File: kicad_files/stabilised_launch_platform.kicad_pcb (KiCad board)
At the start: 2 copper layers, 23 parts, among them J1 Conn_01x03_Male, J2 Conn_01x03_Male, J3 Conn_01x04_Male, Q1 AO3400A, Q2 AO3400A, SW1 SW_Push, U1 MAX7375AXR805, U2 AP7370-33Y, U3 STM32L011F3Px, U4 LIS3DH

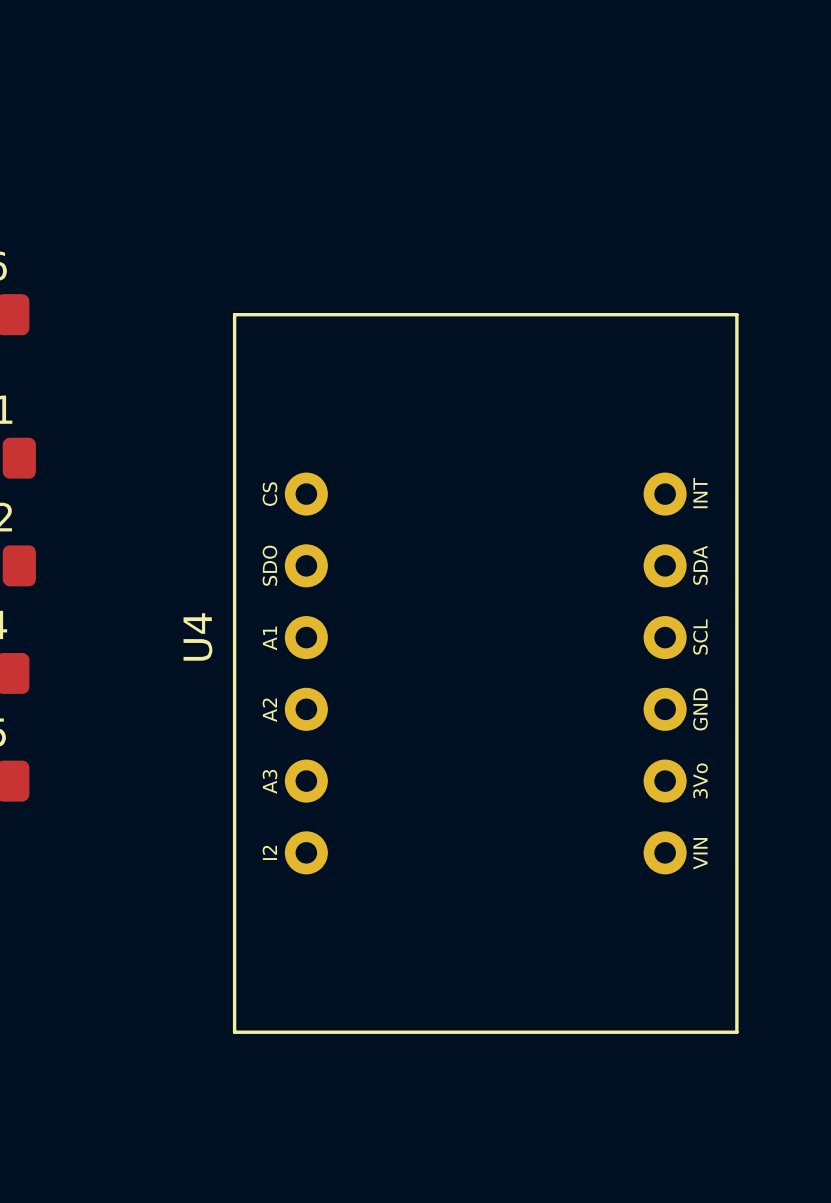
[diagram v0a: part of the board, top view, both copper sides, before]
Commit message: Included custom accelerometer footprint
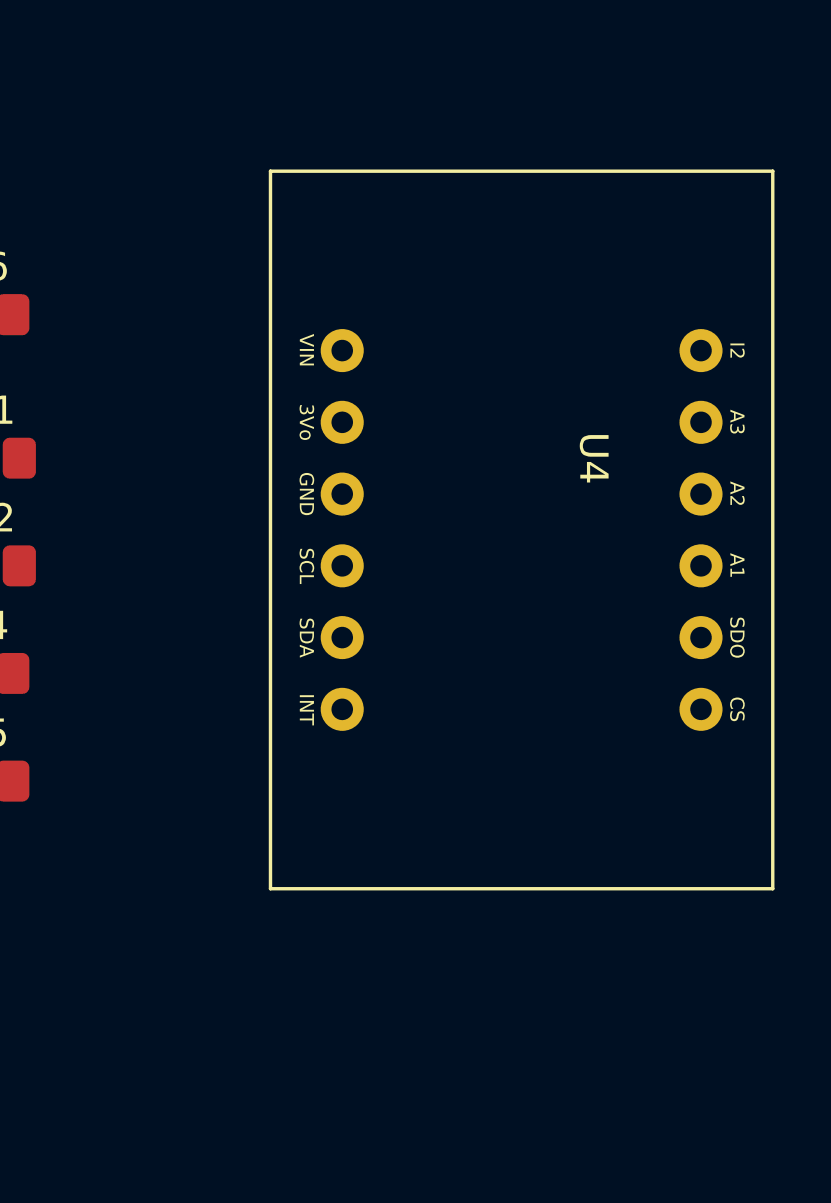
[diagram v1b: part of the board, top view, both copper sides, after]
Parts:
- moved U4 5.24 mm to (153.7, 78.7), turned to -90 degrees
